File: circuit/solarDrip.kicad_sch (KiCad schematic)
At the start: 16 parts, among them J1 DCDC_01x03_Socket, J2 MPPT_01x04_Pin, J3 solar_panel, J4 battery, J5 soil_moisture, J6 water_level, J7 pump, Q1 2N7002E, Q2 2N7002E, U1 ESP32-C3-WROOM-02

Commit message: prepare pcb for edge import
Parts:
- added H1, H2: MountingHole, MountingHole:MountingHole_2.7mm_M2.5_DIN965, symbol Mechanical:MountingHole
- renumbered R4 to R1, R5 to R2, R2 to R3, R3 to R4, R1 to R5

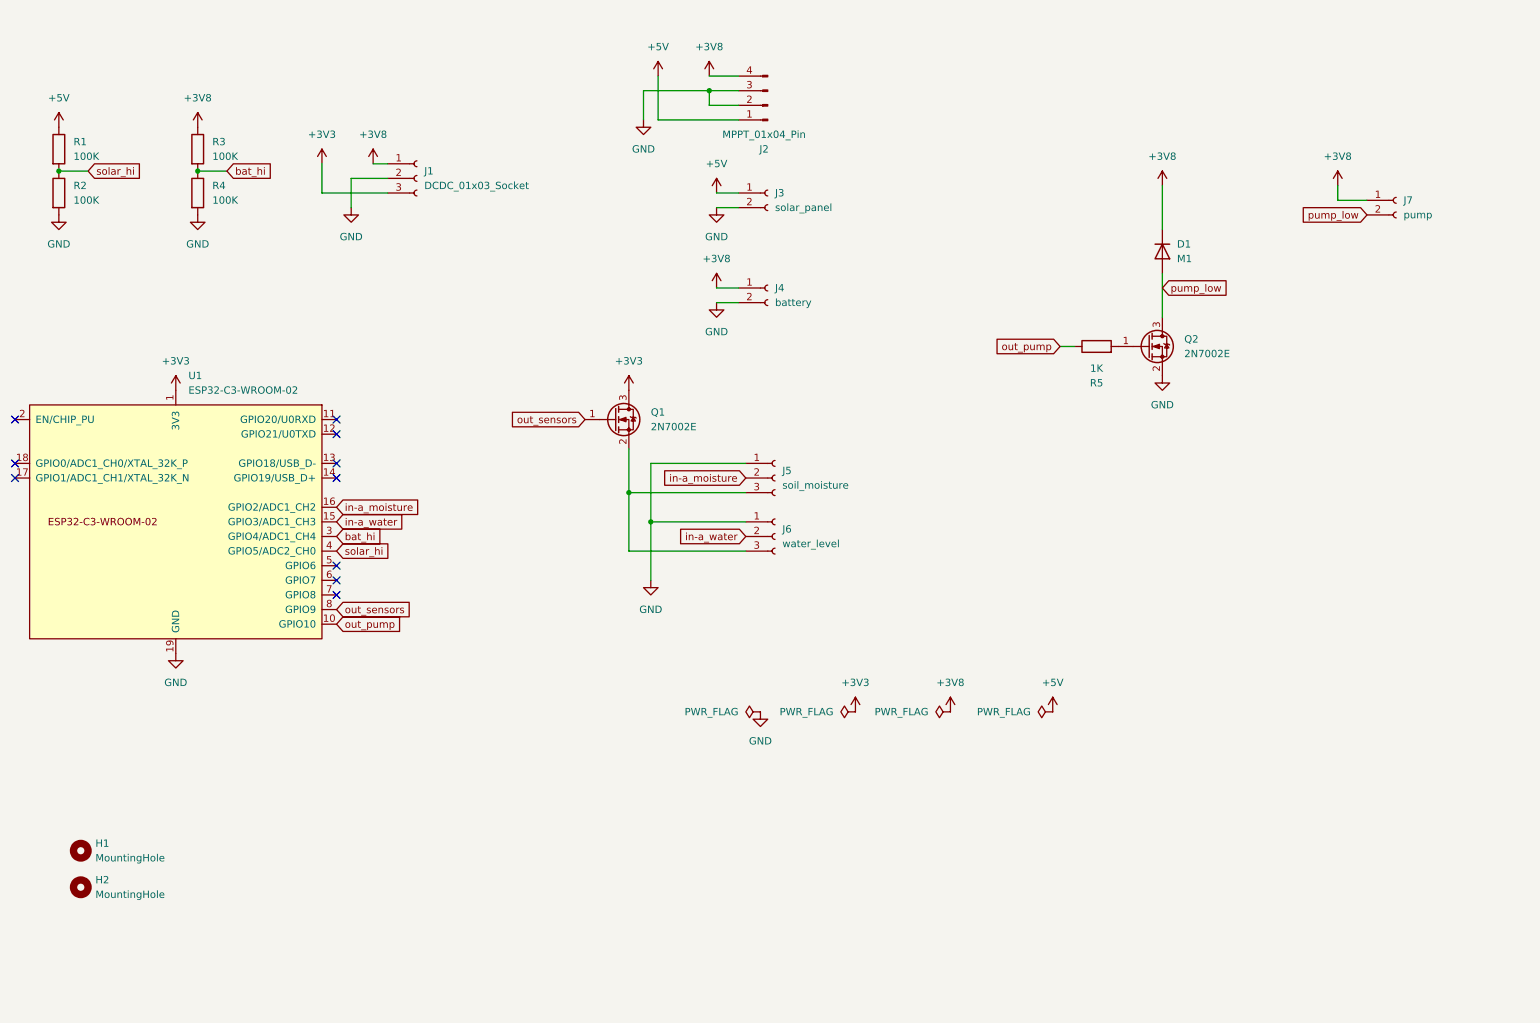
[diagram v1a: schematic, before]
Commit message: add usb charging source
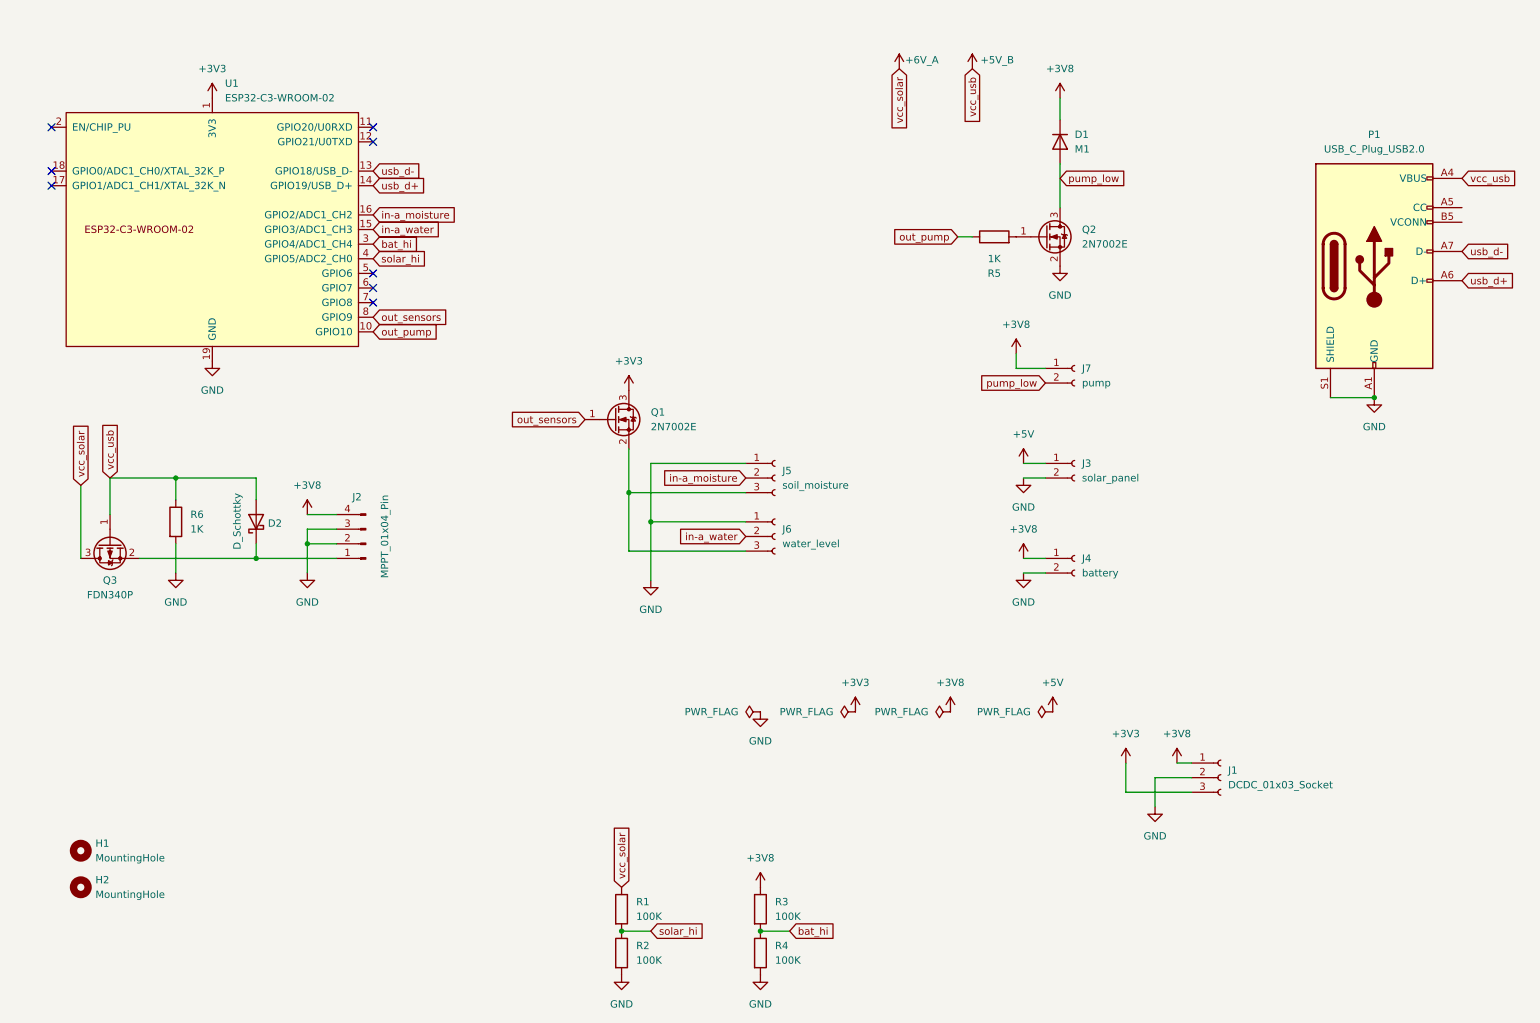
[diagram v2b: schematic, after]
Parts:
- added D2: D_Schottky, symbol Device:D_Schottky
- added P1: USB_C_Plug_USB2.0, symbol Connector:USB_C_Plug_USB2.0
- added Q3: FDN340P, Package_TO_SOT_SMD:SOT-23, symbol Transistor_FET:FDN340P
- added R6: 1K, symbol Device:R
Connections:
- net +5V: no longer J2.1 (Pin_1), R1.1
- net GND: now also P1.A1 (GND), P1.A12 (GND), P1.B1 (GND), P1.B12 (GND), P1.S1 (SHIELD), R6.2
- net usb_d-: now reaches U1.13 (GPIO18/USB_D-)
- net usb_d-: now also P1.A7 (D-)
- net usb_d+: now reaches U1.14 (GPIO19/USB_D+)
- net usb_d+: now also P1.A6 (D+)
- new net: D2.1 (K), J2.1 (Pin_1), Q3.2 (S)
- new net +5V_B: D2.2 (A), P1.A4 (VBUS), P1.A9 (VBUS), P1.B4 (VBUS), P1.B9 (VBUS), Q3.1 (G), R6.1
- new net +6V_A: Q3.3 (D), R1.1
- no-connect marks 10 -> 8
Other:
- moved on the sheet: D1, J1, J2, J3, J4, J7, Q2, R1, R2, R3, R4, R5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

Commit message: cleanup and annotations
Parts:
- P1: footprint (none) -> Connector_USB:USB_C_Plug_Molex_105444
- R6: footprint (none) -> Resistor_SMD:R_0402_1005Metric_Pad0.72x0.64mm_HandSolder
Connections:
- net +5V is gone; now on net +6V_A: J3.1 (Pin_1)
- net vcc_sensor_power: now reaches J5.3 (Pin_3), J6.3 (Pin_3), Q1.2 (S)
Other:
- note added: "Charging: CN3165 Board"
- note added: "Connectors"
- note added: "MCU"
- note added: "Mounting"
- note added: "Power"
- note added: "Pump"
- note added: "Sensors"
- note added: "Stepdown"
- moved on the sheet: D1, D2, H1, H2, J1, J2, J4, J5, J6, J7, P1, Q1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

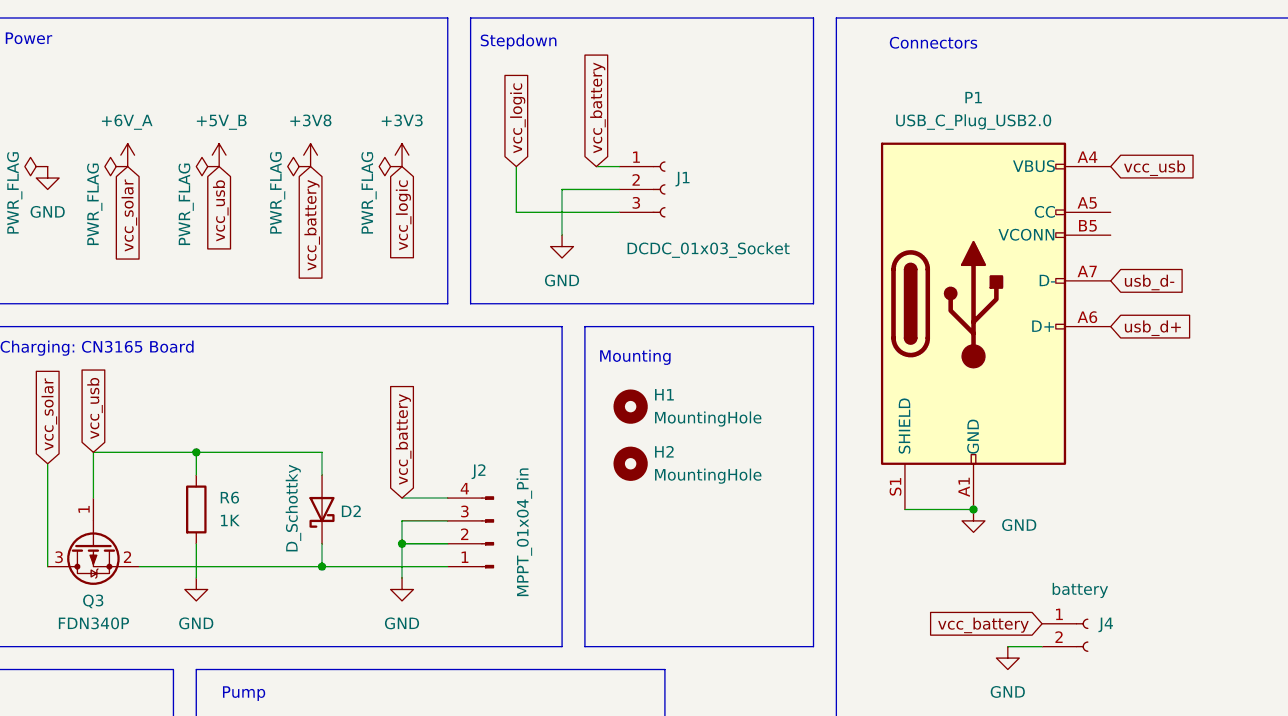
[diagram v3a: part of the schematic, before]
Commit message: replace usb_connector
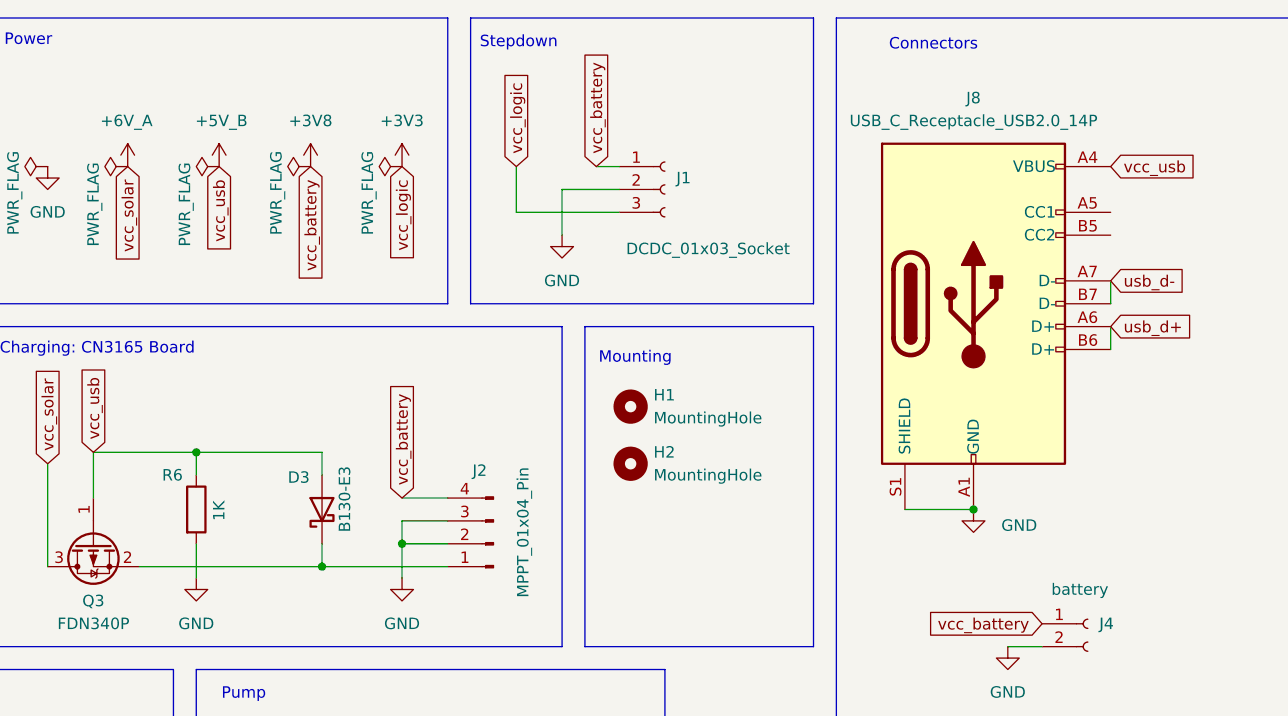
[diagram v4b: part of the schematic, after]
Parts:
- removed D2: D_Schottky, symbol Device:D_Schottky
- removed P1: USB_C_Plug_USB2.0, Connector_USB:USB_C_Plug_Molex_105444, symbol Connector:USB_C_Plug_USB2.0
- added D3: B130-E3, Diode_SMD:D_SMA, symbol Diode:B130-E3
- added J8: USB_C_Receptacle_USB2.0_14P, symbol Connector:USB_C_Receptacle_USB2.0_14P
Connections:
- net +5V_B: now also D3.2 (A), J8.A4 (VBUS), J8.A9 (VBUS), J8.B4 (VBUS), J8.B9 (VBUS)
- net GND: now also J8.A1 (GND), J8.A12 (GND), J8.B1 (GND), J8.B12 (GND), J8.S1 (SHIELD)
- net usb_d+: now also J8.A6 (D+), J8.B6 (D+)
- net usb_d-: now also J8.A7 (D-), J8.B7 (D-)
- net at J2.1 (Pin_1), Q3.2 (S): now also D3.1 (K)
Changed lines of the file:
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@@
 	(paper "A4")
 	(junction
-		(at 219.71 71.12)
-		(diameter 0)
-		(color 0 0 0 0)
-	)
-	(junction
 		(at 133.35 64.77)
 		(diameter 0)
@@
 	)
 	(junction
+		(at 219.71 71.12)
+		(diameter 0)
+		(color 0 0 0 0)
+	)
+	(junction
 		(at 48.26 114.3)
 		(diameter 0)
@@
 	(wire
 		(pts
+			(xy 234.95 45.72) (xy 234.95 48.26)
+		)
+		(stroke
+			(width 0)
+			(type default)
+		)
+	)
+	(wire
+		(pts
 			(xy 173.99 35.56) (xy 180.34 35.56)
 		)
@@
 	(wire
 		(pts
+			(xy 234.95 50.8) (xy 234.95 53.34)
+		)
+		(stroke
+			(width 0)
+			(type default)
+		)
+	)
+	(wire
+		(pts
 			(xy 26.67 114.3) (xy 31.75 114.3)
 		)
@@
 		(on_board yes)
 		(dnp no)
-		(fields_autoplaced yes)
 		(property "Reference" "R6"
-			(at 135.89 69.8499 0)
+			(at 129.54 67.31 0)
 			(effects
 				(font
@@
 		)
 		(property "Value" "1K"
-			(at 135.89 72.3899 0)
+			(at 135.89 72.3899 90)
 			(effects
 				(font
@@
 	)
 	(symbol
-		(lib_id "Connector:USB_C_Plug_USB2.0")
-		(at 219.71 48.26 0)
-		(unit 1)
-		(exclude_from_sim no)
-		(in_bom yes)
-		(on_board yes)
-		(dnp no)
-		(fields_autoplaced yes)
-		(property "Reference" "P1"
-			(at 219.71 25.4 0)
-			(effects
-				(font
-					(size 1.27 1.27)
-				)
-			)
-		)
-		(property "Value" "USB_C_Plug_USB2.0"
-			(at 219.71 27.94 0)
-			(effects
-				(font
-					(size 1.27 1.27)
-				)
-			)
-		)
-		(property "Footprint" "Connector_USB:USB_C_Plug_Molex_105444"
-			(at 223.52 48.26 0)
-			(effects
-				(font
-					(size 1.27 1.27)
-				)
-				(hide yes)
-			)
-		)
-		(property "Datasheet" "https://www.usb.org/sites/default/files/documents/usb_type-c.zip"
-			(at 223.52 48.26 0)
-			(effects
-				(font
-					(size 1.27 1.27)
-				)
-				(hide yes)
-			)
-		)
-		(property "Description" "USB 2.0-only Type-C Plug connector"
-			(at 219.71 48.26 0)
-			(effects
-				(font
-					(size 1.27 1.27)
-				)
-				(hide yes)
-			)
-		)
-		(pin "B1"
-		)
-		(pin "B9"
-		)
-		(pin "A5"
-		)
-		(pin "A12"
-		)
-		(pin "A4"
-		)
-		(pin "B12"
-		)
-		(pin "A6"
-		)
-		(pin "A1"
-		)
-		(pin "A7"
-		)
-		(pin "A9"
-		)
-		(pin "B5"
-		)
-		(pin "S1"
-		)
-		(pin "B4"
-		)
-		(instances
-			(project "solarDrip"
-				(path "/6377a484-fa16-4056-97a2-452f2b7af807"
-					(reference "P1")
-					(unit 1)
-				)
-			)
-		)
-	)
-	(symbol
 		(lib_id "power:+3V3")
 		(at 156.21 33.02 0)
@@
 	)
 	(symbol
-		(lib_id "Device:D_Schottky")
-		(at 147.32 71.12 90)
-		(unit 1)
-		(exclude_from_sim no)
-		(in_bom yes)
-		(on_board yes)
-		(dnp no)
-		(property "Reference" "D2"
-			(at 149.352 71.374 90)
-			(effects
-				(font
-					(size 1.27 1.27)
-				)
-				(justify right)
-			)
-		)
-		(property "Value" "D_Schottky"
-			(at 144.018 75.946 0)
-			(effects
-				(font
-					(size 1.27 1.27)
-				)
-				(justify left)
-			)
-		)
-		(property "Footprint" ""
-			(at 147.32 71.12 0)
-			(effects
-				(font
-					(size 1.27 1.27)
-				)
-				(hide yes)
-			)
-		)
-		(property "Datasheet" "~"
-			(at 147.32 71.12 0)
-			(effects
-				(font
-					(size 1.27 1.27)
-				)
-				(hide yes)
-			)
-		)
-		(property "Description" "Schottky diode"
-			(at 147.32 71.12 0)
-			(effects
-				(font
-					(size 1.27 1.27)
-				)
-				(hide yes)
-			)
-		)
-		(pin "1"
-		)
-		(pin "2"
-		)
-		(instances
-			(project "solarDrip"
-				(path "/6377a484-fa16-4056-97a2-452f2b7af807"
-					(reference "D2")
-					(unit 1)
-				)
-			)
-		)
-	)
-	(symbol
 		(lib_id "power:+5V")
 		(at 125.73 33.02 0)
@@
 	)
 	(symbol
+		(lib_id "Diode:B130-E3")
+		(at 147.32 71.12 90)
+		(unit 1)
+		(exclude_from_sim no)
+		(in_bom yes)
+		(on_board yes)
+		(dnp no)
+		(property "Reference" "D3"
+			(at 143.51 67.564 90)
+			(effects
+				(font
+					(size 1.27 1.27)
+				)
+				(justify right)
+			)
+		)
+		(property "Value" "B130-E3"
+			(at 149.86 66.294 0)
+			(effects
+				(font
+					(size 1.27 1.27)
+				)
+				(justify right)
+			)
+		)
+		(property "Footprint" "Diode_SMD:D_SMA"
+			(at 151.765 71.12 0)
+			(effects
+				(font
+					(size 1.27 1.27)
+				)
+				(hide yes)
+			)
+		)
+		(property "Datasheet" "http://www.vishay.com/docs/88946/b120.pdf"
+			(at 147.32 71.12 0)
+			(effects
+				(font
+					(size 1.27 1.27)
+				)
+				(hide yes)
+			)
+		)
+		(property "Description" "30V 1A Schottky Barrier Rectifier Diode, SMA(DO-214AC)"
+			(at 147.32 71.12 0)
+			(effects
+				(font
+					(size 1.27 1.27)
+				)
+				(hide yes)
+			)
+		)
+		(pin "1"
+		)
+		(pin "2"
+		)
+		(instances
+			(project "solarDrip"
+				(path "/6377a484-fa16-4056-97a2-452f2b7af807"
+					(reference "D3")
+					(unit 1)
+				)
+			)
+		)
+	)
+	(symbol
 		(lib_id "power:GND")
 		(at 223.52 101.6 0)
@@
 					(unit 1)
 				)
+			)
+		)
+	)
+	(symbol
+		(lib_id "Connector:USB_C_Receptacle_USB2.0_14P")
+		(at 219.71 48.26 0)
+		(unit 1)
+		(exclude_from_sim no)
+		(in_bom yes)
+		(on_board yes)
+		(dnp no)
+		(fields_autoplaced yes)
+		(property "Reference" "J8"
+			(at 219.71 25.4 0)
+			(effects
+				(font
+					(size 1.27 1.27)
+				)
+			)
+		)
+		(property "Value" "USB_C_Receptacle_USB2.0_14P"
+			(at 219.71 27.94 0)
+			(effects
+				(font
+					(size 1.27 1.27)
+				)
+			)
+		)
+		(property "Footprint" ""
+			(at 223.52 48.26 0)
+			(effects
+				(font
+					(size 1.27 1.27)
+				)
+				(hide yes)
+			)
+		)
+		(property "Datasheet" "https://www.usb.org/sites/default/files/documents/usb_type-c.zip"
+			(at 223.52 48.26 0)
+			(effects
+				(font
+					(size 1.27 1.27)
+				)
+				(hide yes)
+			)
+		)
+		(property "Description" "USB 2.0-only 14P Type-C Receptacle connector"
+			(at 219.71 48.26 0)
+			(effects
+				(font
+					(size 1.27 1.27)
+				)
+				(hide yes)
+			)
+		)
+		(pin "B9"
+		)
+		(pin "A6"
+		)
+		(pin "A9"
+		)
+		(pin "A7"
+		)
+		(pin "A5"
+		)
+		(pin "B6"
+		)
+		(pin "B7"
+		)
+		(pin "A4"
+		)
+		(pin "B1"
+		)
+		(pin "A12"
+		)
+		(pin "B12"
+		)
+		(pin "A1"
+		)
+		(pin "B4"
+		)
+		(pin "B5"
+		)
+		(pin "S1"
+		)
+		(instances
+			(project "solarDrip"
+				(path "/6377a484-fa16-4056-97a2-452f2b7af807"
+					(reference "J8")
+					(unit 1)
+				)

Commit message: various updates
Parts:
- added D2: D_Zener, symbol Device:D_Zener
- added R7, R8: 5k1, symbol Device:R
- J8: footprint (none) -> Connector_USB:USB_C_Receptacle_G-Switch_GT-USB-7010ASV
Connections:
- net GND: now also D2.2 (A), R7.1, R8.1
- net pump_low: now also D2.1 (K)
- net at J8.A5 (CC1): now also R8.2
- net at J8.B5 (CC2): now also R7.2
